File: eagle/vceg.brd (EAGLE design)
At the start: 100 x 80 mm, 58 parts, among them IC1 4052N, IC2 4001N, IC3 TL074P, IC5 CA3080E, Q1 2N3906INLINE, Q2 2N3906INLINE, U1 POWER

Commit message: decoupling caps
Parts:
- added C4, C5, C6, C7, C8, C9: .1, rcl:C025-024X044
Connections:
- removed net VCC: IC1.16
- removed net VDD: IC2.14
- removed net VEE: IC1.7
- removed net VSS: IC2.7
- net +12V: now also C4.1, C5.1, C6.1, C8.1, IC1.16, IC2.14
- net -12V: now also C7.2, C9.2
- net GND: now also C4.2, C5.2, C6.2, C7.1, C8.2, C9.1, IC1.7, IC2.7
- net N$25: now also C3.2; no longer LFO_SW_1.MP
- net N$32: now also LFO_SW_2.MP; no longer C3.1
- net N$35: now also C3.1, LFO_SW_1.MP; no longer C3.2, LFO_SW_2.MP
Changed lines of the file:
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@@
 <element name="U1" library="eurorack" package="POWER_16" value="POWER" x="21.59" y="71.12"/>
 <element name="IC5" library="ota" package="DIL08" value="CA3080E" x="7.62" y="-17.78"/>
+<element name="C4" library="rcl" package="C025-024X044" value=".1" x="2.54" y="-27.94"/>
+<element name="C5" library="rcl" package="C025-024X044" value=".1" x="2.54" y="-33.02"/>
+<element name="C6" library="rcl" package="C025-024X044" value=".1" x="2.54" y="-38.1"/>
+<element name="C7" library="rcl" package="C025-024X044" value=".1" x="2.54" y="-43.18"/>
+<element name="C8" library="rcl" package="C025-024X044" value=".1" x="2.54" y="-48.26"/>
+<element name="C9" library="rcl" package="C025-024X044" value=".1" x="2.54" y="-53.34"/>
 </elements>
 <signals>
-<signal name="VEE">
-<contactref element="IC1" pad="7"/>
-</signal>
 <signal name="GND">
 <contactref element="IC1" pad="8"/>
@@
 <contactref element="R32" pad="P$1"/>
 <contactref element="IC3" pad="12"/>
-<wire x1="67.31" y1="62.23" x2="72.39" y2="67.31" width="0" layer="19" extent="1-1"/>
-<wire x1="72.39" y1="58.42" x2="67.31" y2="62.23" width="0" layer="19" extent="1-1"/>
-<wire x1="72.39" y1="55.88" x2="72.39" y2="58.42" width="0" layer="19" extent="1-1"/>
-<wire x1="80.01" y1="54.61" x2="72.39" y2="55.88" width="0" layer="19" extent="1-1"/>
+<contactref element="IC1" pad="7"/>
+<contactref element="IC2" pad="7"/>
+<contactref element="C4" pad="2"/>
+<contactref element="C5" pad="2"/>
+<contactref element="C6" pad="2"/>
+<contactref element="C7" pad="1"/>
+<contactref element="C9" pad="1"/>
+<contactref element="C8" pad="2"/>
+<wire x1="80.01" y1="54.61" x2="95.25" y2="55.88" width="0" layer="19" extent="1-1"/>
+<wire x1="72.39" y1="55.88" x2="80.01" y2="54.61" width="0" layer="19" extent="1-1"/>
+<wire x1="72.39" y1="58.42" x2="72.39" y2="55.88" width="0" layer="19" extent="1-1"/>
+<wire x1="67.31" y1="62.23" x2="72.39" y2="58.42" width="0" layer="19" extent="1-1"/>
+<wire x1="72.39" y1="67.31" x2="67.31" y2="62.23" width="0" layer="19" extent="1-1"/>
 <wire x1="53.34" y1="57.15" x2="67.31" y2="62.23" width="0" layer="19" extent="1-1"/>
 <wire x1="41.91" y1="55.88" x2="53.34" y2="57.15" width="0" layer="19" extent="1-1"/>
@@
 <wire x1="68.58" y1="38.1" x2="73.66" y2="38.1" width="0" layer="19" extent="1-1"/>
 <wire x1="76.2" y1="30.48" x2="73.66" y2="38.1" width="0" layer="19" extent="1-1"/>
-<wire x1="81.28" y1="30.48" x2="76.2" y2="30.48" width="0" layer="19" extent="1-1"/>
-<wire x1="80.01" y1="20.32" x2="81.28" y2="30.48" width="0" layer="19" extent="1-1"/>
+<wire x1="78.74" y1="30.48" x2="76.2" y2="30.48" width="0" layer="19" extent="1-1"/>
+<wire x1="81.28" y1="30.48" x2="78.74" y2="30.48" width="0" layer="19" extent="1-1"/>
+<wire x1="80.01" y1="20.32" x2="78.74" y2="30.48" width="0" layer="19" extent="1-1"/>
 <wire x1="85.17" y1="2.54" x2="80.01" y2="20.32" width="0" layer="19" extent="1-1"/>
 <wire x1="64.85" y1="2.54" x2="85.17" y2="2.54" width="0" layer="19" extent="1-1"/>
@@
 <wire x1="3.89" y1="2.54" x2="24.21" y2="2.54" width="0" layer="19" extent="1-1"/>
 <wire x1="34.29" y1="27.94" x2="16.51" y2="48.26" width="0" layer="19" extent="1-1"/>
-</signal>
-<signal name="VCC">
-<contactref element="IC1" pad="16"/>
-</signal>
-<signal name="VSS">
-<contactref element="IC2" pad="7"/>
-</signal>
-<signal name="VDD">
-<contactref element="IC2" pad="14"/>
+<wire x1="3.81" y1="-27.94" x2="3.89" y2="2.54" width="0" layer="19" extent="1-1"/>
+<wire x1="3.81" y1="-33.02" x2="3.81" y2="-27.94" width="0" layer="19" extent="1-1"/>
+<wire x1="3.81" y1="-38.1" x2="3.81" y2="-33.02" width="0" layer="19" extent="1-1"/>
+<wire x1="1.27" y1="-43.18" x2="3.81" y2="-38.1" width="0" layer="19" extent="1-1"/>
+<wire x1="3.81" y1="-48.26" x2="1.27" y2="-43.18" width="0" layer="19" extent="1-1"/>
+<wire x1="1.27" y1="-53.34" x2="3.81" y2="-48.26" width="0" layer="19" extent="1-1"/>
 </signal>
 <signal name="+12V">
@@
 <contactref element="IC3" pad="4"/>
 <contactref element="IC5" pad="7"/>
-<wire x1="63.5" y1="43.18" x2="63.5" y2="48.26" width="0" layer="19" extent="1-1"/>
-<wire x1="50.8" y1="38.1" x2="63.5" y2="43.18" width="0" layer="19" extent="1-1"/>
+<contactref element="IC1" pad="16"/>
+<contactref element="IC2" pad="14"/>
+<contactref element="C4" pad="1"/>
+<contactref element="C5" pad="1"/>
+<contactref element="C6" pad="1"/>
+<contactref element="C8" pad="1"/>
+<wire x1="63.5" y1="43.18" x2="87.63" y2="40.64" width="0" layer="19" extent="1-1"/>
+<wire x1="63.5" y1="48.26" x2="63.5" y2="43.18" width="0" layer="19" extent="1-1"/>
+<wire x1="63.5" y1="38.1" x2="63.5" y2="43.18" width="0" layer="19" extent="1-1"/>
+<wire x1="50.8" y1="38.1" x2="63.5" y2="38.1" width="0" layer="19" extent="1-1"/>
 <wire x1="46.99" y1="38.1" x2="50.8" y2="38.1" width="0" layer="19" extent="1-1"/>
 <wire x1="31.75" y1="35.56" x2="46.99" y2="38.1" width="0" layer="19" extent="1-1"/>
@@
 <wire x1="13.89" y1="2.54" x2="6.35" y2="34.29" width="0" layer="19" extent="1-1"/>
 <wire x1="6.35" y1="-13.97" x2="13.89" y2="2.54" width="0" layer="19" extent="1-1"/>
+<wire x1="1.27" y1="-27.94" x2="6.35" y2="-13.97" width="0" layer="19" extent="1-1"/>
+<wire x1="1.27" y1="-33.02" x2="1.27" y2="-27.94" width="0" layer="19" extent="1-1"/>
+<wire x1="1.27" y1="-38.1" x2="1.27" y2="-33.02" width="0" layer="19" extent="1-1"/>
+<wire x1="1.27" y1="-48.26" x2="1.27" y2="-38.1" width="0" layer="19" extent="1-1"/>
 <wire x1="34.21" y1="2.54" x2="13.89" y2="2.54" width="0" layer="19" extent="1-1"/>
 <wire x1="54.53" y1="2.54" x2="34.21" y2="2.54" width="0" layer="19" extent="1-1"/>
@@
 <contactref element="IC3" pad="11"/>
 <contactref element="IC5" pad="4"/>
+<contactref element="C7" pad="2"/>
+<contactref element="C9" pad="2"/>
 <wire x1="15.24" y1="69.85" x2="15.24" y2="72.39" width="0" layer="19" extent="1-1"/>
 <wire x1="31.75" y1="27.94" x2="15.24" y2="69.85" width="0" layer="19" extent="1-1"/>
 <wire x1="11.43" y1="-21.59" x2="31.75" y2="27.94" width="0" layer="19" extent="1-1"/>
+<wire x1="3.81" y1="-43.18" x2="11.43" y2="-21.59" width="0" layer="19" extent="1-1"/>
+<wire x1="3.81" y1="-53.34" x2="3.81" y2="-43.18" width="0" layer="19" extent="1-1"/>
 </signal>
 <signal name="N$4">
@@
 <contactref element="IC2" pad="8"/>
 <contactref element="R25" pad="P$2"/>
-<contactref element="LFO_SW_1" pad="MP"/>
-<wire x1="73.66" y1="71.12" x2="78.74" y2="71.12" width="0" layer="19" extent="1-1"/>
-<wire x1="77.47" y1="62.23" x2="78.74" y2="71.12" width="0" layer="19" extent="1-1"/>
+<contactref element="C3" pad="2"/>
+<wire x1="77.47" y1="62.23" x2="73.66" y2="71.12" width="0" layer="19" extent="1-1"/>
 <wire x1="87.63" y1="55.88" x2="77.47" y2="62.23" width="0" layer="19" extent="1-1"/>
+<wire x1="20.32" y1="25.4" x2="77.47" y2="62.23" width="0" layer="19" extent="1-1"/>
 </signal>
 <signal name="N$27">
@@
 <signal name="N$32">
 <contactref element="IC3" pad="8"/>
-<contactref element="C3" pad="1"/>
-<wire x1="22.86" y1="25.4" x2="24.13" y2="27.94" width="0" layer="19" extent="1-1"/>
+<contactref element="LFO_SW_2" pad="MP"/>
+<wire x1="15.24" y1="25.4" x2="24.13" y2="27.94" width="0" layer="19" extent="1-1"/>
 </signal>
 <signal name="N$34">
@@
 <wire x1="46.99" y1="27.94" x2="41.91" y2="45.72" width="0" layer="19" extent="1-1"/>
 <wire x1="29.21" y1="27.94" x2="46.99" y2="27.94" width="0" layer="19" extent="1-1"/>
-</signal>
-<signal name="N$35">
-<contactref element="C3" pad="2"/>
-<contactref element="LFO_SW_2" pad="MP"/>
-<wire x1="15.24" y1="25.4" x2="20.32" y2="25.4" width="0" layer="19" extent="1-1"/>
 </signal>
 <signal name="N$33">
@@
 <wire x1="88.9" y1="24.13" x2="92.71" y2="24.13" width="0" layer="19" extent="1-1"/>
 </signal>
-<signal name="N$39">
+<signal name="N$40">
+<contactref element="IC3" pad="14"/>
+<contactref element="IC3" pad="13"/>
+<wire x1="36.83" y1="27.94" x2="39.37" y2="27.94" width="0" layer="19" extent="1-1"/>
+</signal>
+<signal name="N$21">
+<contactref element="Q1" pad="C"/>
+<contactref element="IC5" pad="5"/>
+<wire x1="11.43" y1="-13.97" x2="60.96" y2="55.88" width="0" layer="19" extent="1-1"/>
+</signal>
+<signal name="N$41">
+<contactref element="IC5" pad="3"/>
+<contactref element="IC1" pad="13"/>
+<wire x1="8.89" y1="-21.59" x2="71.12" y2="38.1" width="0" layer="19" extent="1-1"/>
+</signal>
+<signal name="N$23">
 <contactref element="U1" pad="15"/>
 <contactref element="U1" pad="16"/>
@@
 <wire x1="33.02" y1="69.85" x2="33.02" y2="72.39" width="0" layer="19" extent="1-1"/>
 </signal>
-<signal name="N$40">
-<contactref element="IC3" pad="14"/>
-<contactref element="IC3" pad="13"/>
-<wire x1="36.83" y1="27.94" x2="39.37" y2="27.94" width="0" layer="19" extent="1-1"/>
-</signal>
-<signal name="N$21">
-<contactref element="Q1" pad="C"/>
-<contactref element="IC5" pad="5"/>
-<wire x1="11.43" y1="-13.97" x2="60.96" y2="55.88" width="0" layer="19" extent="1-1"/>
-</signal>
-<signal name="N$41">
-<contactref element="IC5" pad="3"/>
-<contactref element="IC1" pad="13"/>
-<wire x1="8.89" y1="-21.59" x2="71.12" y2="38.1" width="0" layer="19" extent="1-1"/>
+<signal name="N$35">
+<contactref element="LFO_SW_1" pad="MP"/>
+<contactref element="C3" pad="1"/>
+<wire x1="22.86" y1="25.4" x2="78.74" y2="71.12" width="0" layer="19" extent="1-1"/>
 </signal>
 </signals>

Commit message: started board over
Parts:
- moved C9 131.1 mm to (71.1, 58.4), turned to 90 degrees
- moved C4 125.8 mm to (94.0, 58.4), turned to 90 degrees
- moved C6 113.2 mm to (67.1, 54.9), turned to 90 degrees
- moved C7 107.2 mm to (48.8, 53.6), turned to 90 degrees
- moved C5 90.2 mm to (66.8, 30.2), turned to 270 degrees
- moved IC5 88.4 mm to (58.7, 54.4), turned to 180 degrees
- moved LFO_SW_2 85.8 mm to (89.4, 68.6)
- moved TG_SWB_3 82.6 mm to (90.2, 42.9)
- moved C8 82.5 mm to (7.62, 34.0), turned to 270 degrees
- moved R27 74.0 mm to (93.5, 30.5), turned to 270 degrees
- moved R18 72.2 mm to (9.14, 63.2)
- moved R32 71.4 mm to (82.8, 45.7), turned to 0 degrees
- moved R26 70.6 mm to (79.0, 21.1)
- moved R31 66.7 mm to (82.8, 50.5), turned to 0 degrees
- moved RATE 63.2 mm to (80.0, 9.14), turned to 0 degrees
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
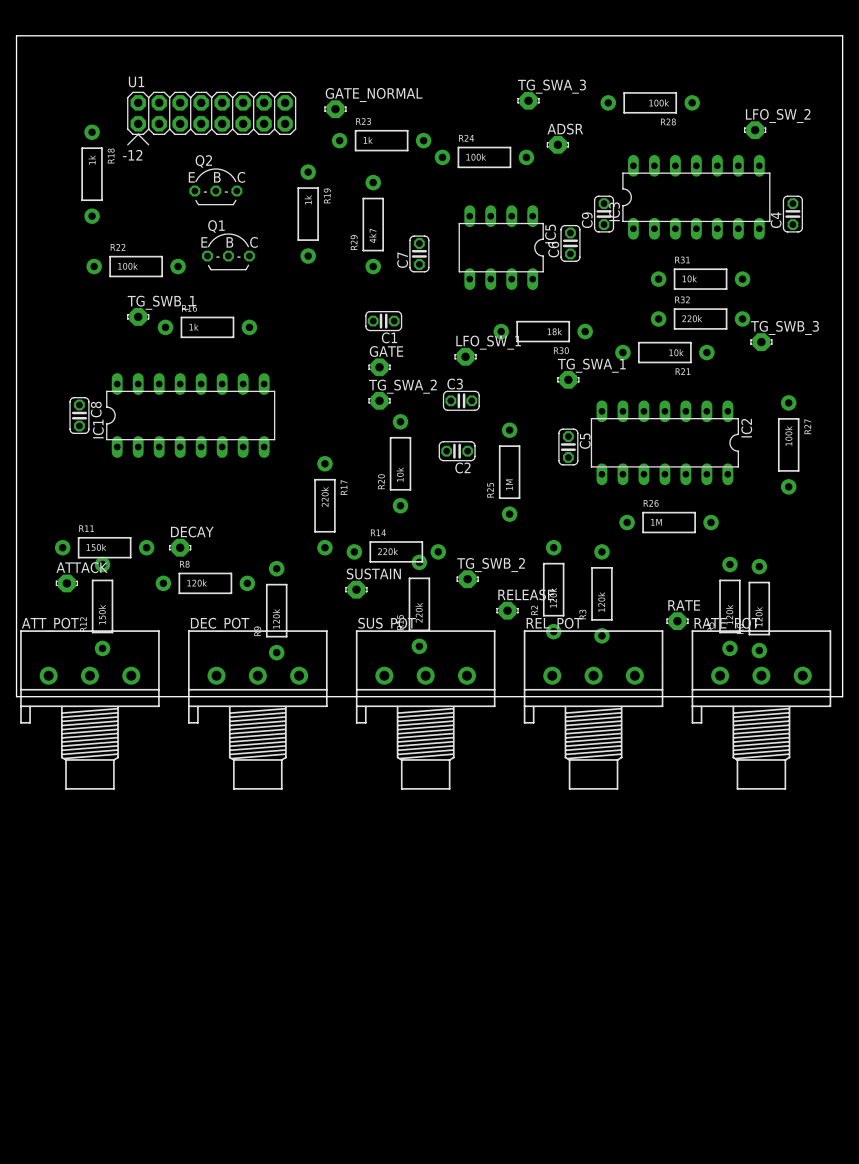
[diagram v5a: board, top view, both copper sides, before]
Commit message: completed layout with five flyers
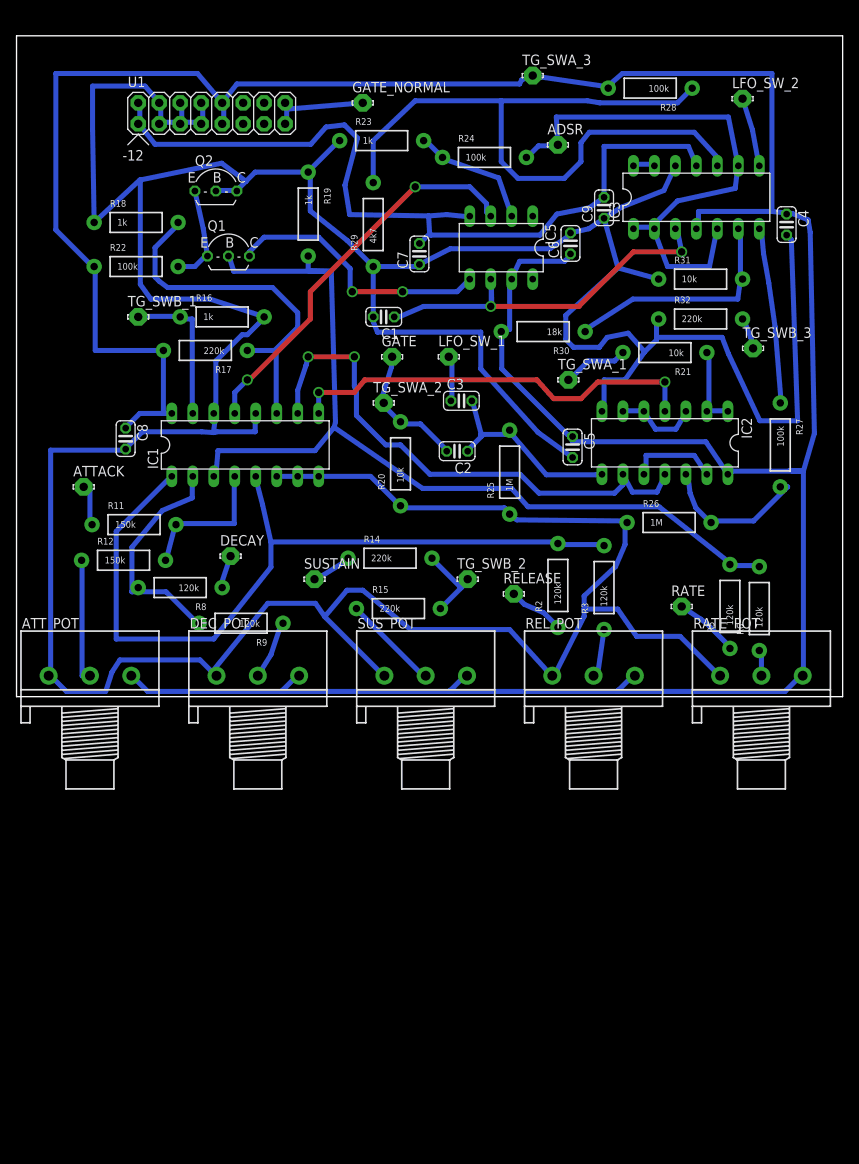
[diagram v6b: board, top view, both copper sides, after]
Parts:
- moved R17 23.7 mm to (22.9, 41.9), turned to 180 degrees
- moved ATTACK 11.9 mm to (8.13, 25.4)
- moved R18 7.91 mm to (14.5, 57.4), turned to 0 degrees
- moved IC1 7.50 mm to (27.7, 30.5)
- moved C8 6.25 mm to (13.2, 31.2)
- moved DECAY 6.18 mm to (25.9, 17.0)
- moved R12 6.14 mm to (13.0, 16.5), turned to 0 degrees
- moved SUSTAIN 5.24 mm to (36.1, 14.2)
- moved R9 4.58 mm to (27.2, 8.89), turned to 180 degrees
- moved R11 4.52 mm to (14.2, 20.8)
- moved LFO_SW_2 4.10 mm to (87.9, 72.4)
- moved GATE_NORMAL 3.39 mm to (41.9, 71.9)
- moved TG_SWA_3 3.09 mm to (62.5, 75.2)
- moved R8 3.09 mm to (19.8, 13.2), turned to 180 degrees
- moved R15 2.59 mm to (46.2, 10.7), turned to 0 degrees
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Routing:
- net GND: track 0.00 -> 545.1 mm
- net +12V: track 0.00 -> 397.9 mm
- net N$5: track 0.00 -> 113.6 mm
- net -12V: track 0.00 -> 101.8 mm
- net N$2: track 0.00 -> 97.3 mm
- net N$34: track 0.00 -> 86.8 mm
- net N$26: track 0.00 -> 66.5 mm
- net N$17: track 0.00 -> 65.4 mm, vias 0 -> 2
- net N$20: track 0.00 -> 50.6 mm, vias 0 -> 2
- net N$41: track 0.00 -> 47.8 mm, vias 0 -> 2
- net N$28: track 0.00 -> 47.8 mm, vias 0 -> 2
- net N$16: track 0.00 -> 43.7 mm
- net N$21: track 0.00 -> 32.8 mm, vias 0 -> 2
- net N$33: track 0.00 -> 28.8 mm
- net N$8: track 0.00 -> 28.4 mm
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
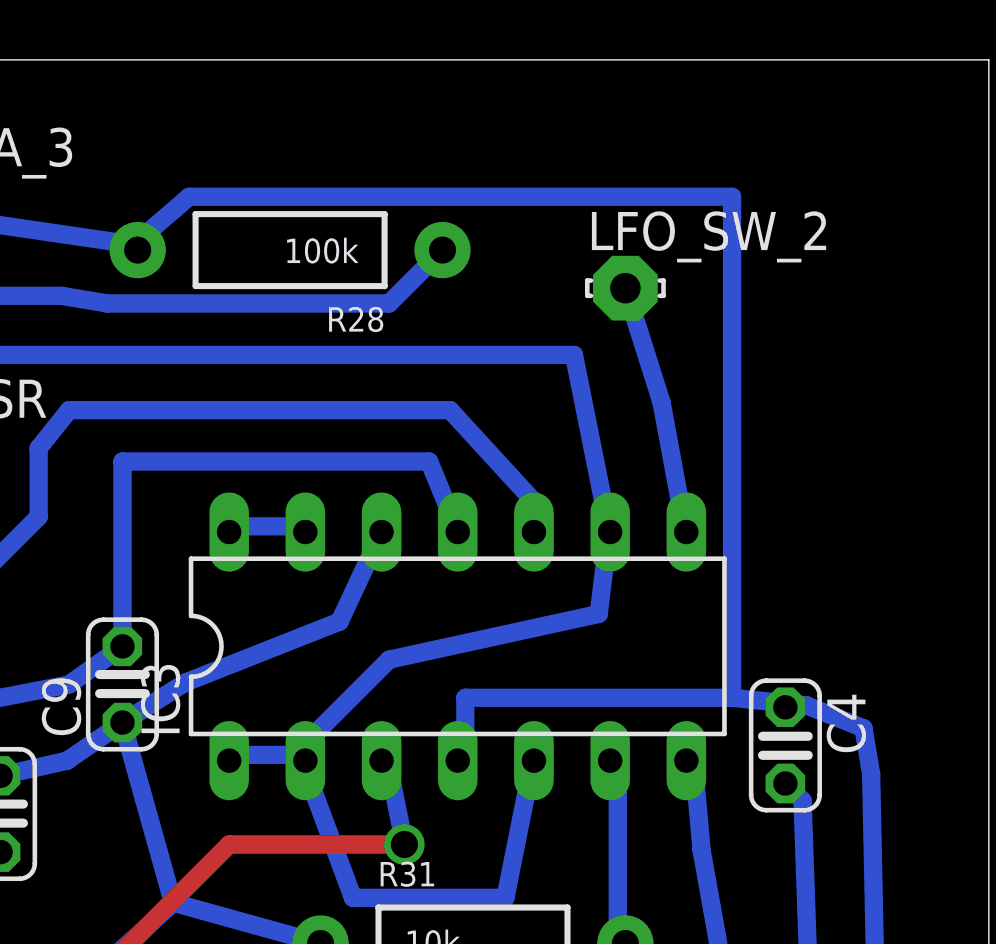
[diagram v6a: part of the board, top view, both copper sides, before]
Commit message: gcode for first prototype
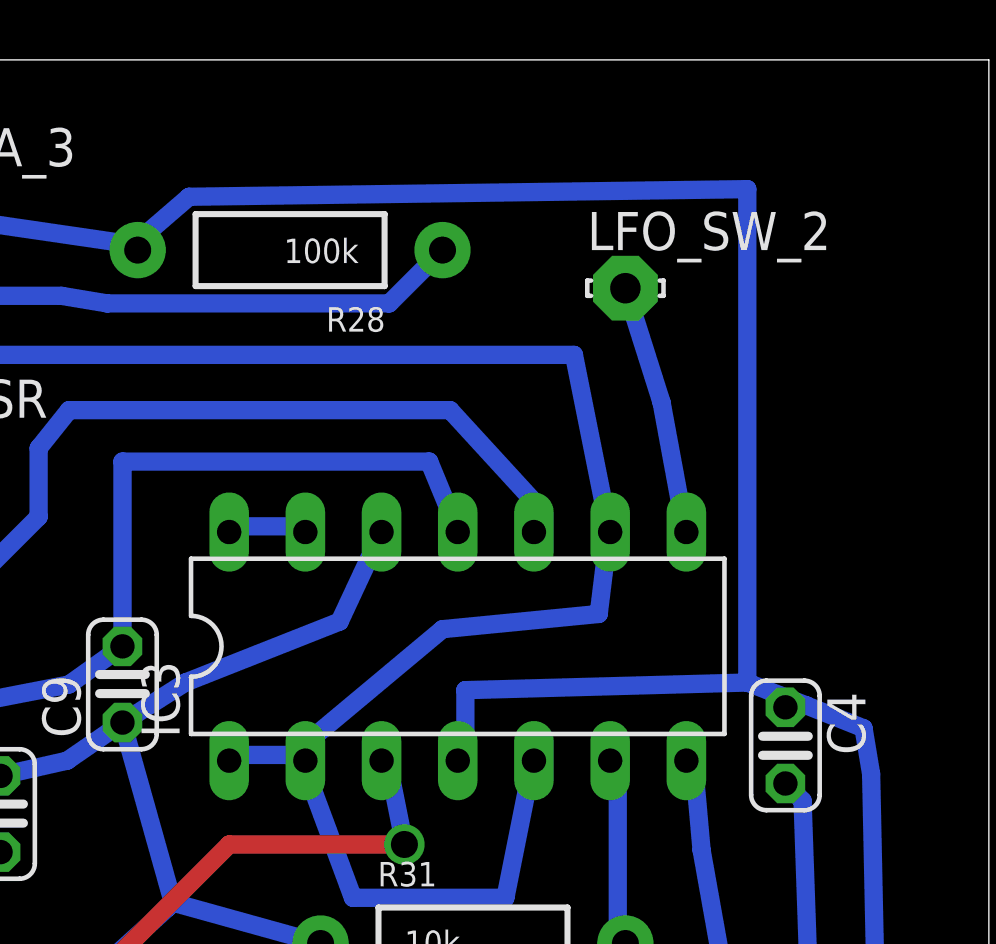
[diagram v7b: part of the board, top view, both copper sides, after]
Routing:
- net +12V: track 397.9 -> 398.6 mm
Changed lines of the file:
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@@
 <wire x1="17.78" y1="41.91" x2="9.525" y2="41.91" width="0.6096" layer="16"/>
 <wire x1="9.525" y1="52.07" x2="9.398" y2="52.07" width="0.6096" layer="16"/>
-<wire x1="82.55" y1="58.7375" x2="82.55" y2="56.8325" width="0.6096" layer="16"/>
-<wire x1="93.9165" y1="58.4835" x2="91.44" y2="58.7375" width="0.6096" layer="16"/>
-<wire x1="91.44" y1="58.7375" x2="82.55" y2="58.7375" width="0.6096" layer="16"/>
+<wire x1="82.55" y1="58.9915" x2="82.55" y2="56.8325" width="0.6096" layer="16"/>
+<wire x1="93.9165" y1="58.4835" x2="91.948" y2="59.2455" width="0.6096" layer="16"/>
+<wire x1="91.948" y1="59.2455" x2="82.55" y2="58.9915" width="0.6096" layer="16"/>
 <wire x1="93.218" y1="58.42" x2="93.9165" y2="58.4835" width="0.6096" layer="16"/>
 <wire x1="82.55" y1="56.8325" x2="82.296" y2="56.642" width="0.6096" layer="16"/>
@@
 <wire x1="61.1505" y1="74.676" x2="60.8965" y2="74.168" width="0.6096" layer="16"/>
 <wire x1="61.1505" y1="74.676" x2="62.484" y2="75.184" width="0.6096" layer="16"/>
-<wire x1="91.44" y1="75.438" x2="91.44" y2="58.7375" width="0.6096" layer="16"/>
-<wire x1="73.3425" y1="75.438" x2="91.44" y2="75.438" width="0.6096" layer="16"/>
+<wire x1="91.948" y1="75.692" x2="91.948" y2="59.2455" width="0.6096" layer="16"/>
+<wire x1="73.3425" y1="75.438" x2="91.948" y2="75.692" width="0.6096" layer="16"/>
 <wire x1="71.501" y1="73.8505" x2="73.3425" y2="75.438" width="0.6096" layer="16"/>
 <wire x1="71.501" y1="73.8505" x2="71.628" y2="73.66" width="0.6096" layer="16"/>
@@
 <wire x1="77.1525" y1="56.515" x2="77.216" y2="56.642" width="0.6096" layer="16"/>
 <wire x1="86.995" y1="61.5315" x2="87.3125" y2="64.135" width="0.6096" layer="16"/>
-<wire x1="80.01" y1="60.0075" x2="86.995" y2="61.5315" width="0.6096" layer="16"/>
-<wire x1="77.1525" y1="57.15" x2="80.01" y2="60.0075" width="0.6096" layer="16"/>
+<wire x1="81.788" y1="61.0235" x2="86.995" y2="61.5315" width="0.6096" layer="16"/>
+<wire x1="77.1525" y1="57.15" x2="81.788" y2="61.0235" width="0.6096" layer="16"/>
 <wire x1="87.3125" y1="64.135" x2="87.376" y2="64.262" width="0.6096" layer="16"/>
 <wire x1="77.1525" y1="57.15" x2="77.216" y2="56.642" width="0.6096" layer="16"/>
